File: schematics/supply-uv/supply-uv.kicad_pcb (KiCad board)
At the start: 2 copper layers, 110 x 108 mm, 84 parts, among them J1 Conn_01x02_Pin, J2 Conn_01x01_Pin, J3 CW2B-10A-T, K1 SRD-12VDC-SL-C, Q1 IRLML5203, U1 ICE2PCS01, U2 TL331, U3 R7731, U4 EL817, U5 TL432DBZ, Y1 B32022A3223M000

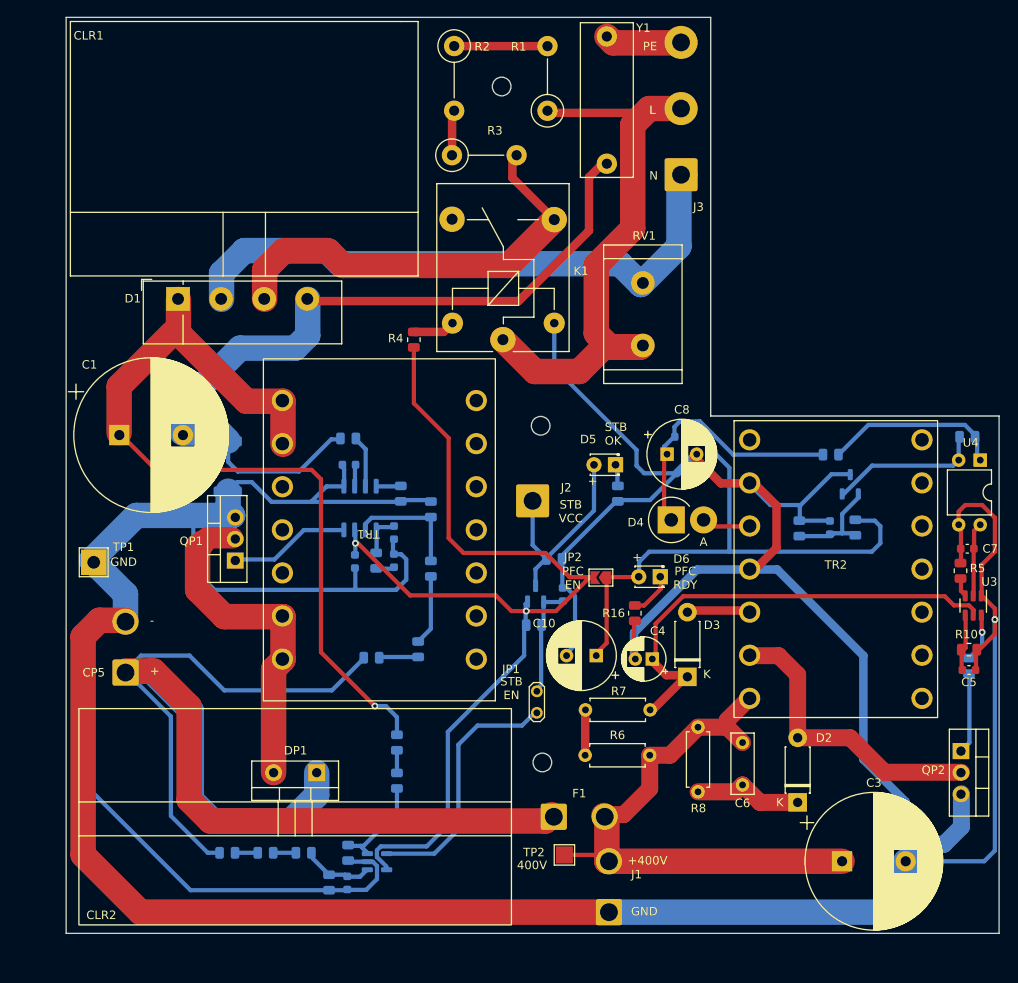
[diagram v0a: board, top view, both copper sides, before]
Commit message: UV board size changed to 100x100 to reduce production price
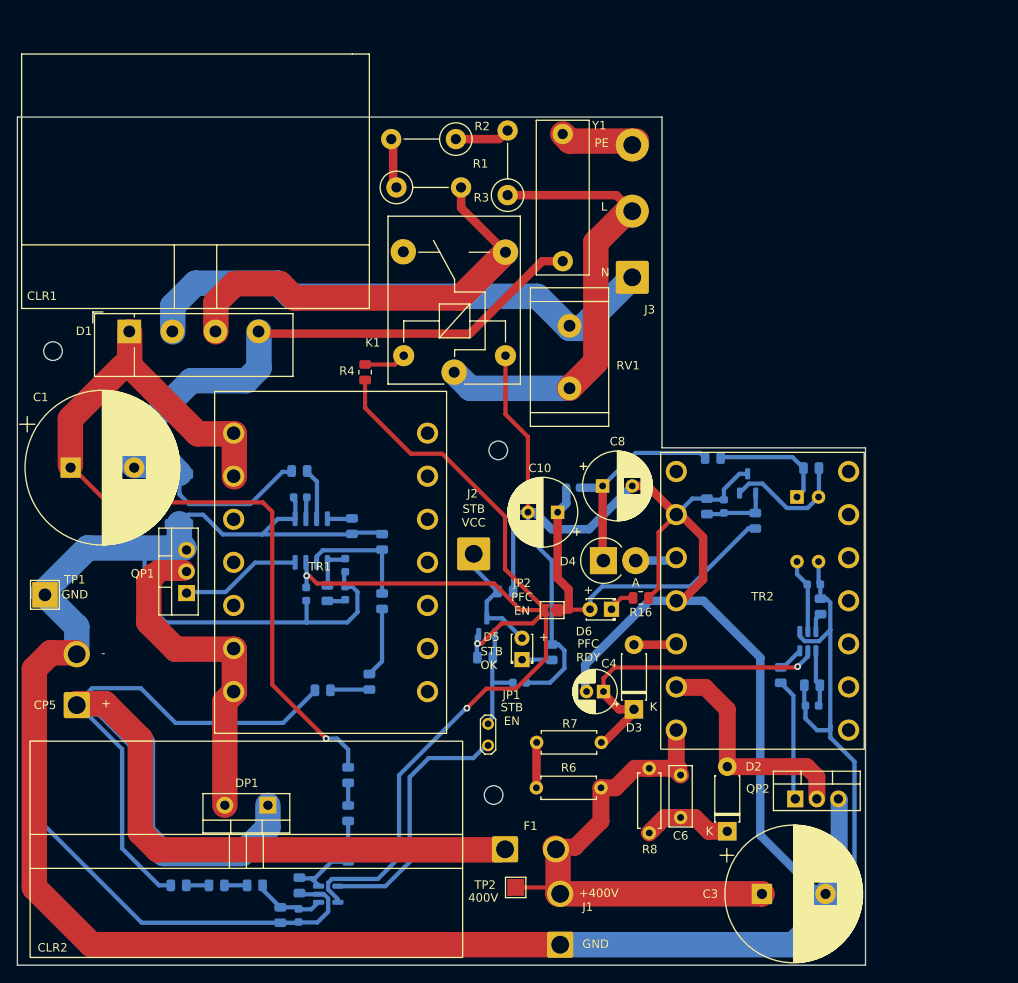
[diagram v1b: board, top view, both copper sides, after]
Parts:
- C5, C7, R10, R5, U3, U4: moved to B.Cu
- moved H1 61.4 mm to (64.2, 77.6)
- moved D5 25.5 mm to (119.5, 114.0), turned to 90 degrees
- moved R9 22.2 mm to (150.0, 115.8)
- moved U4 22.0 mm to (151.9, 94.8)
- moved QP2 20.3 mm to (151.7, 130.4), turned to 0 degrees
- moved R11 20.3 mm to (123.0, 113.1), turned to -90 degrees
- moved U3 19.9 mm to (153.2, 111.8)
- moved C5 19.0 mm to (153.7, 119.4), turned to 0 degrees
- moved R10 19.0 mm to (153.7, 117.0), turned to 0 degrees
- moved R13 18.8 mm to (153.6, 91.4), turned to 180 degrees
- moved C7 18.6 mm to (153.9, 105.1), turned to 180 degrees
- moved C10 17.5 mm to (123.7, 96.6)
- moved R5 17.0 mm to (154.7, 107.7)
- moved L1 14.1 mm to (125.5, 93.7), turned to 180 degrees
- moved R12 13.9 mm to (142.0, 90.2)
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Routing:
- net Net-(D6-A): track 66.5 -> 43.4 mm
- net /Input power with filter/STARTUP_PROTECT_IN: track 73.5 -> 54.2 mm
- net Net-(D3-K): track 54.9 -> 37.2 mm, vias 0 -> 1
- net /Input power with filter/HV_GND: track 560.3 -> 545.5 mm, vias 1 -> 0
- net /Input power with filter/PFC_VCC: track 121.5 -> 134.1 mm, vias 2 -> 3
- net /Standby Supply/V_STANDBY: track 24.6 -> 14.4 mm
- net Net-(D2-A): track 35.1 -> 27.6 mm
- net Net-(J3-Pin_1): track 70.4 -> 63.0 mm
- net Net-(R12-Pad1): track 21.0 -> 13.9 mm
- net Net-(D4-K): track 30.8 -> 24.7 mm
- net /Input power with filter/OUT_400V: track 65.8 -> 60.0 mm
- net /Input power with filter/VOUT_PRE_GND: track 94.0 -> 88.5 mm
- net Net-(R1-Pad2): track 11.4 -> 6.52 mm
- net Net-(QP2-G): track 9.53 -> 14.1 mm
- net Net-(U5-REF): track 11.3 -> 8.07 mm
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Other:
- board size 110 x 108 mm -> 100 x 100 mm

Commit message: Boards prepared to order
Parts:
- R1, R2, R3: footprint Resistor_THT:R_Axial_DIN0411_L9.9mm_D3.6mm_P7.62mm_Vertical -> Resistor_THT:R_Axial_DIN0516_L15.5mm_D5.0mm_P7.62mm_Vertical
- moved R3 0.61 mm to (105.0, 58.8)
- moved K1 0.55 mm to (111.3, 80.6)
- moved R2 0.47 mm to (111.5, 53.0)
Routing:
- net Net-(R2-Pad2): track 5.09 -> 6.30 mm
- net /Input power with filter/STARTUP_PROTECT_OUT: track 51.3 -> 50.6 mm
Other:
- board text added: "0,0000 mm / 0,0000 mm"
- board text added: "0,3000 mm"
- board text added: "1,6000 mm"
- board text added: "100,0000 mm x 100,0000 mm"
- board text added: "2"
- board text added: "None"
- board text added: "Габариты платы:"
- board text added: "Количество слоёв меди:"
- board text added: "Контроль импеданса:"
- board text added: "Краевой соединитель:"
- board text added: "Метал. торцы:"
- board text added: "Мин. дорожка/зазор:"
- board text added: "Мин. сверло:"
- board text added: "Нет"
- board text added: "Периферийные полу-отверстия:"
- board text added: "Покрытие меди:"
- board text added: "Толщина платы:"
- board text added: "ХАРАКТЕРИСТИКИ ПЛАТЫ"

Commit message: Found and fixed issues in schematics.
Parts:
- removed TP2: 400V, TestPoint:TestPoint_Pad_2.0x2.0mm
- added CLR3: HS077@20x15x10mm, Library:HS-077, F.Cu at (77.9, 103.9)
- added R19: 1R, Resistor_SMD:R_2512_6332Metric, B.Cu at (160.0, 130.0)
- added RP17: 0.12, Resistor_SMD:R_2512_6332Metric, B.Cu at (78.8, 92.6)
- added TP3: Supply VCC, TestPoint:TestPoint_Pad_2.0x2.0mm, F.Cu at (130.1, 113.4)
- added TP4: STB VCC, TestPoint:TestPoint_Pad_2.0x2.0mm, F.Cu at (126.7, 96.8)
- C4: value 22 uF@50V -> 22 uF; footprint Capacitor_THT:CP_Radial_D5.0mm_P2.00mm -> Capacitor_SMD:C_1210_3225Metric; moved to B.Cu
- R1, R2, R3: footprint Resistor_THT:R_Axial_DIN0516_L15.5mm_D5.0mm_P7.62mm_Vertical -> Varistor:RV_Disc_D12mm_W5.8mm_P7.5mm
- R12: value 1K -> 150
- R13: value 1K2 -> NOT INSTALLED
- R14: value 20K -> 22K
- R15: value 4K7 -> 2K2
- R18: value 200K -> 100K
- R6, R7: value 1M -> 300K
- R8: value 305K -> 220K
- RP1: value 20K -> 33K
- RP10, RP9: value 750K -> 680K
- RP11: value 750K -> 620K
- RP12: value 17K -> 15K
- RP16: value 60K -> 62K
- RP2: value 0.01 -> 0.12
- RP8: value 70K -> 75K
- TR1: value ETD 34/17/11@N87@s=5mm N25@1mm*2 -> ETD 34/17/11@N87@s=3.3mm N27@1mm*2
- moved C4 24.0 mm to (152.8, 113.9), turned to 0 degrees
- moved C5 10.3 mm to (158.0, 110.0), turned to 180 degrees
- moved R9 8.19 mm to (152.8, 108.1)
- moved R2 7.94 mm to (116.0, 46.5), turned to -90 degrees
- moved C1 6.77 mm to (69.1, 85.2)
- moved C3 6.71 mm to (150.8, 135.6)
- moved H2 6.71 mm to (119.0, 83.0)
- moved H3 6.59 mm to (119.0, 124.0)
- moved C6 6.53 mm to (141.2, 126.8)
- moved C9 6.53 mm to (146.3, 90.1)
- moved CLR2 6.53 mm to (90.0, 130.8)
- moved CP1 6.53 mm to (96.3, 89.0)
- moved CP3 6.53 mm to (101.7, 97.0)
- moved D2 6.53 mm to (146.7, 128.4)
- moved D3 6.53 mm to (135.7, 114.0)
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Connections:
- C4 pad 1: Net-(D3-K) -> /Input power with filter/HV_GND
- C4 pad 2: /Input power with filter/HV_GND -> Net-(D3-K)
- QP2 pad 3: /Input power with filter/HV_GND -> Net-(QP2-S)
- R10 pad 1: /Input power with filter/HV_GND -> Net-(QP2-S)
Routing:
- net /Input power with filter/HV_GND: track 545.4 -> 509.5 mm, vias 0 -> 2
- net /Input power with filter/STARTUP_PROTECT_OUT: track 50.6 -> 69.9 mm
- net Net-(QP2-S): track 0.00 -> 17.0 mm
- net Net-(DP1-A): track 39.8 -> 26.7 mm
- net /Input power with filter/VOUT_PRE_GND: track 88.5 -> 95.6 mm
- net Net-(QP1-G): track 14.6 -> 20.5 mm
- net /Input power with filter/OUT_400V: track 60.0 -> 55.2 mm
- net Net-(D3-K): track 37.2 -> 41.8 mm
- net Net-(DP1-K): track 162.2 -> 166.4 mm
- net Net-(QP2-G): track 14.1 -> 15.9 mm
- net /Standby Supply/V_STANDBY: track 14.4 -> 12.8 mm
- net /Input power with filter/VOUT_PRE_PFC: track 99.7 -> 98.2 mm
- net Net-(U3-CS): track 6.52 -> 5.60 mm
- net Net-(U1-ISENSE): track 6.03 -> 5.12 mm
- net Net-(K1-Pad5): track 4.57 -> 3.83 mm
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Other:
- outline, holes or cut-outs redrawn
- board text added: "Supply board#1 v1.1"
- board text removed: "400V"
- board text removed: "Supply board#1 v1.0"

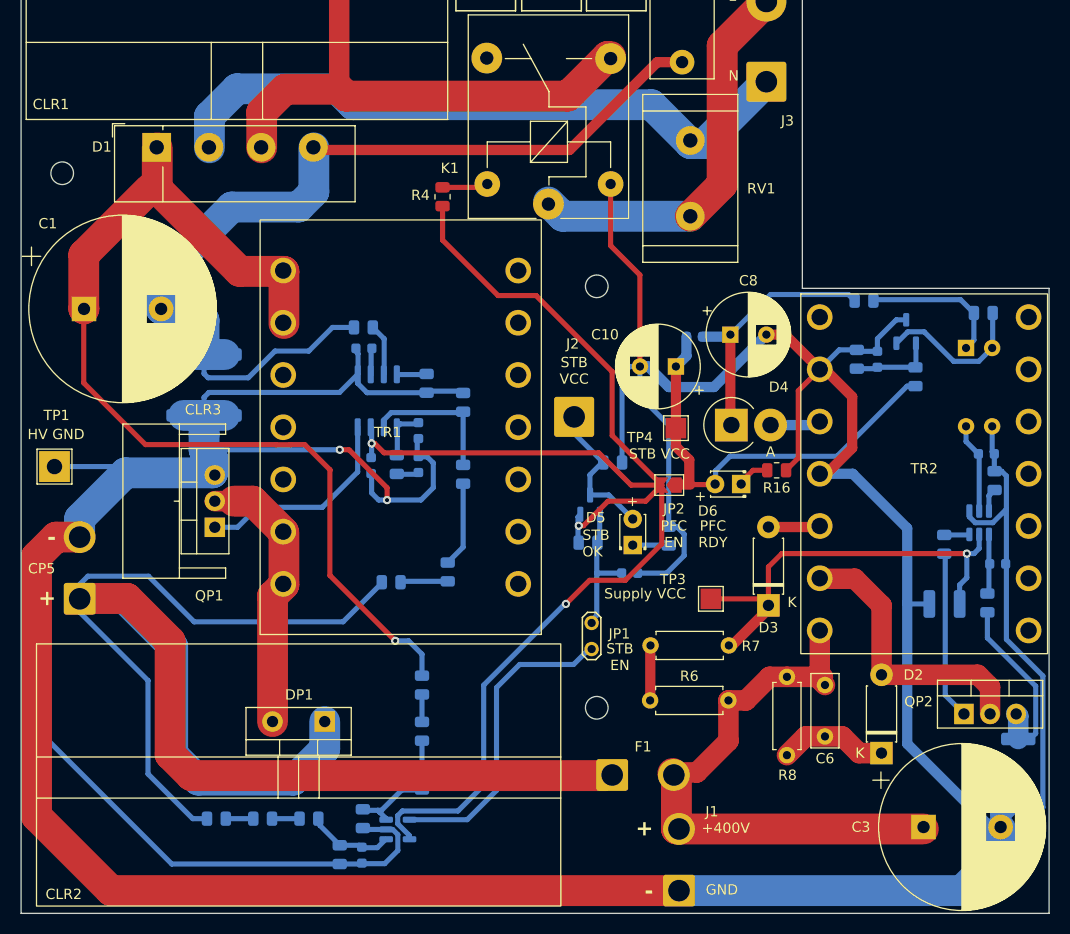
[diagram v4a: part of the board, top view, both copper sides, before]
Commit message: debugging DCDC converters... Standby supply works fine (noise level = 1,7%). At now Starting to debug PFC module
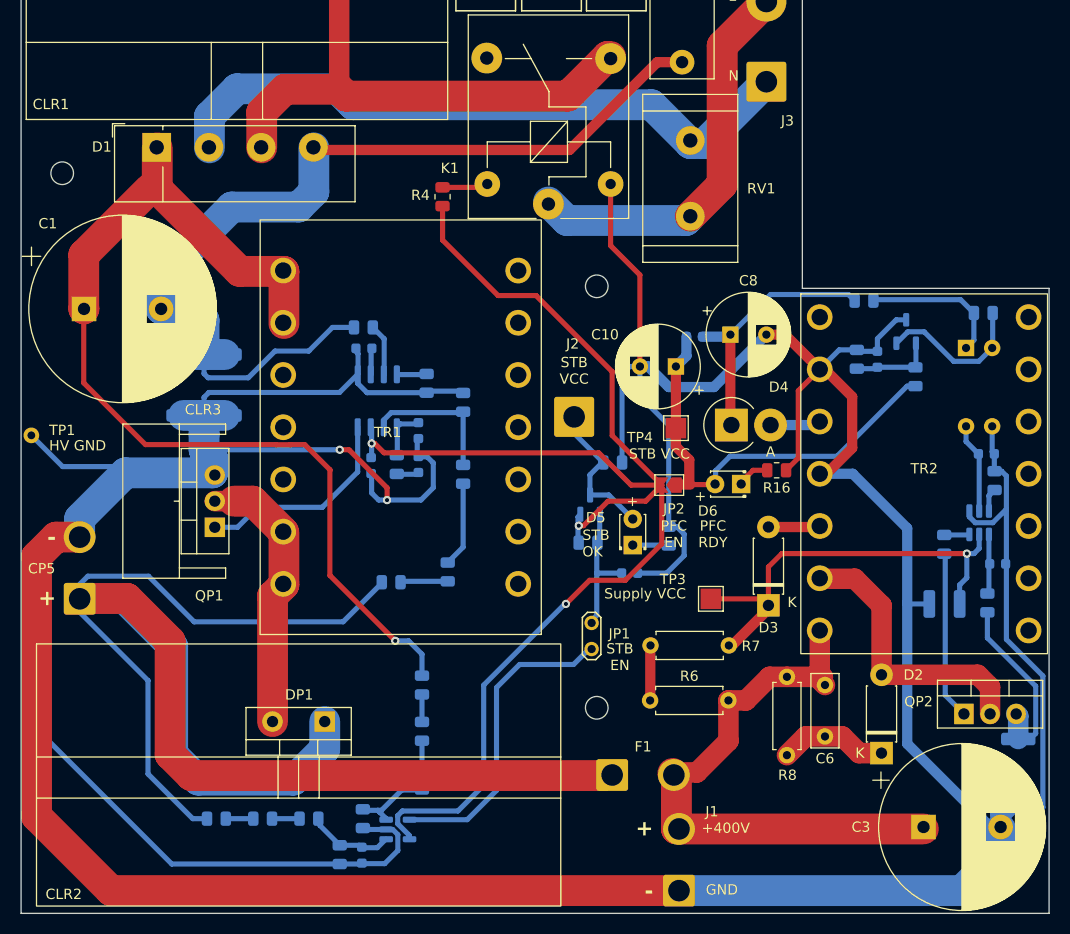
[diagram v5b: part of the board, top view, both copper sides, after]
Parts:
- R10: value 10K -> 5
- R12: value 150 -> 2K
- R13: value NOT INSTALLED -> 2K
- R14: value 22K -> 39K
- R15: value 2K2 -> 3K
- R4: value 50 -> 150
- R6, R7: value 300K -> 1M
- RP16: value 62K -> 68K
- TP1: footprint TestPoint:TestPoint_THTPad_3.0x3.0mm_Drill1.5mm -> Library:TestPoint_Plated_Hole_D1.0mm
- TR2: value ETD 29/16/10@N87@s=0.2mm N56/13/9@0.5mm -> ETD 29/16/10@N87@s=0.2mm N41/8/9@0.5mm
- moved TP1 3.78 mm to (64.0, 97.5)
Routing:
- net /Input power with filter/HV_GND: track 509.5 -> 513.0 mm
- net Net-(DP1-K): track 166.4 -> 165.1 mm
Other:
- board text added: "Supply board#1 v1.3"
- board text removed: "Supply board#1 v1.1"
